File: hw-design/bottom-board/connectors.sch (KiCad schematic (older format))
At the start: 27 parts, among them J1 RJ45_LEDS, J2 JACK_TRS_6PINS, J3 JACK_TRS_6PINS, J4 JACK_TRS_6PINS, J5 JACK_TRS_6PINS, J6 JACK_TRS_6PINS, P5 BARREL_JACK, P6 CONN_02X10, P7 CONN_01X10, P9 CONN_01X03

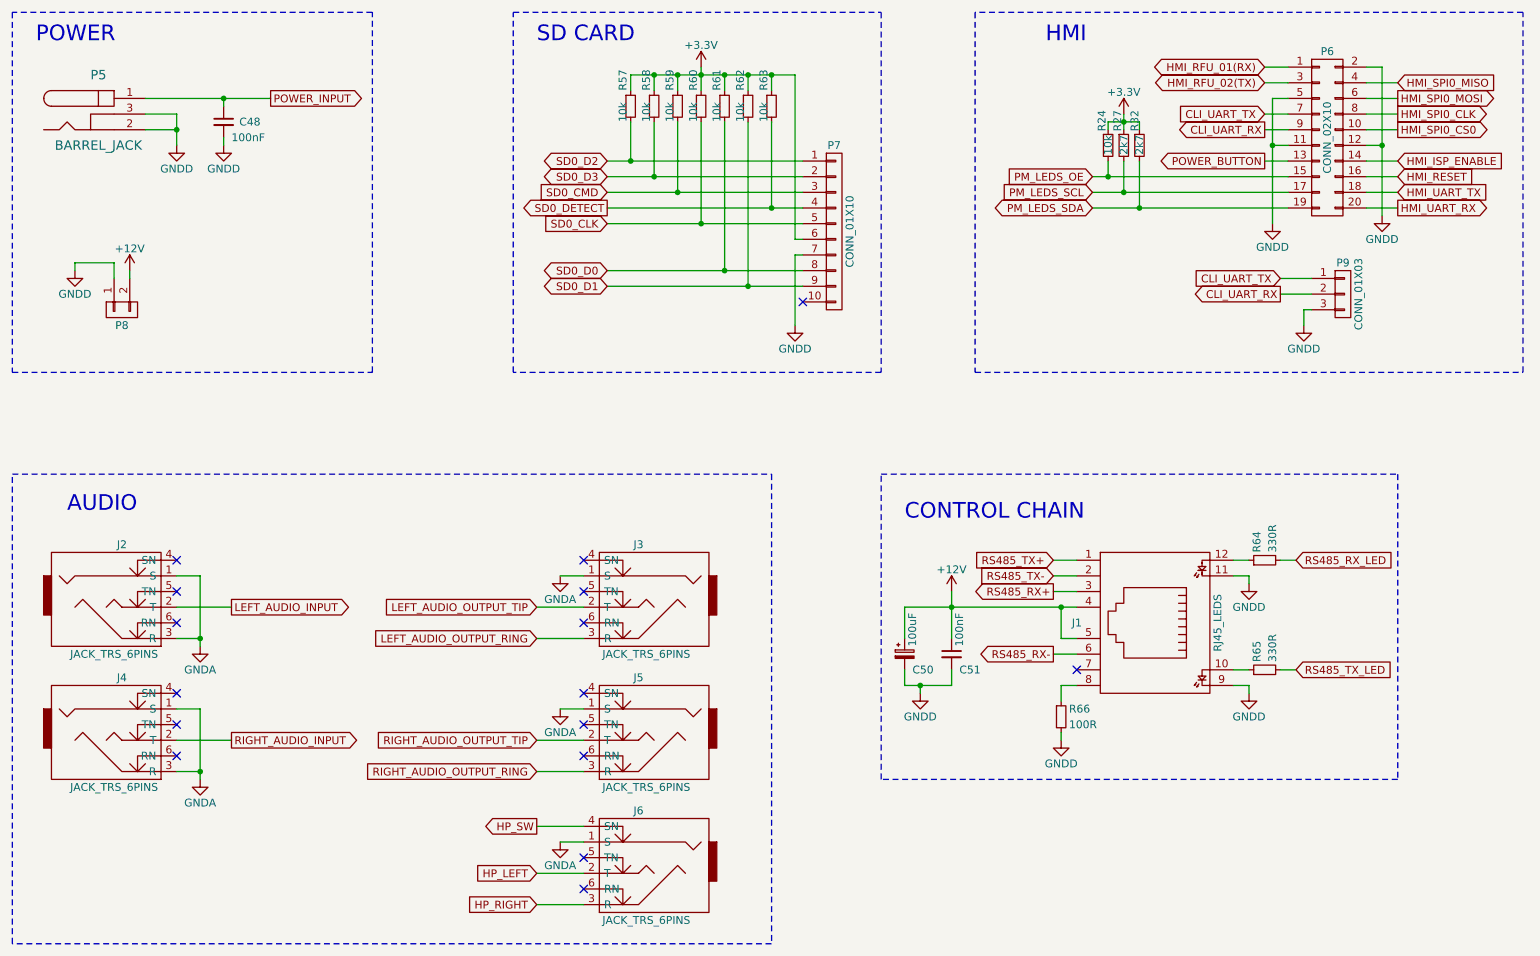
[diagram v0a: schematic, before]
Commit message: sch,bottom-board: ERC passing
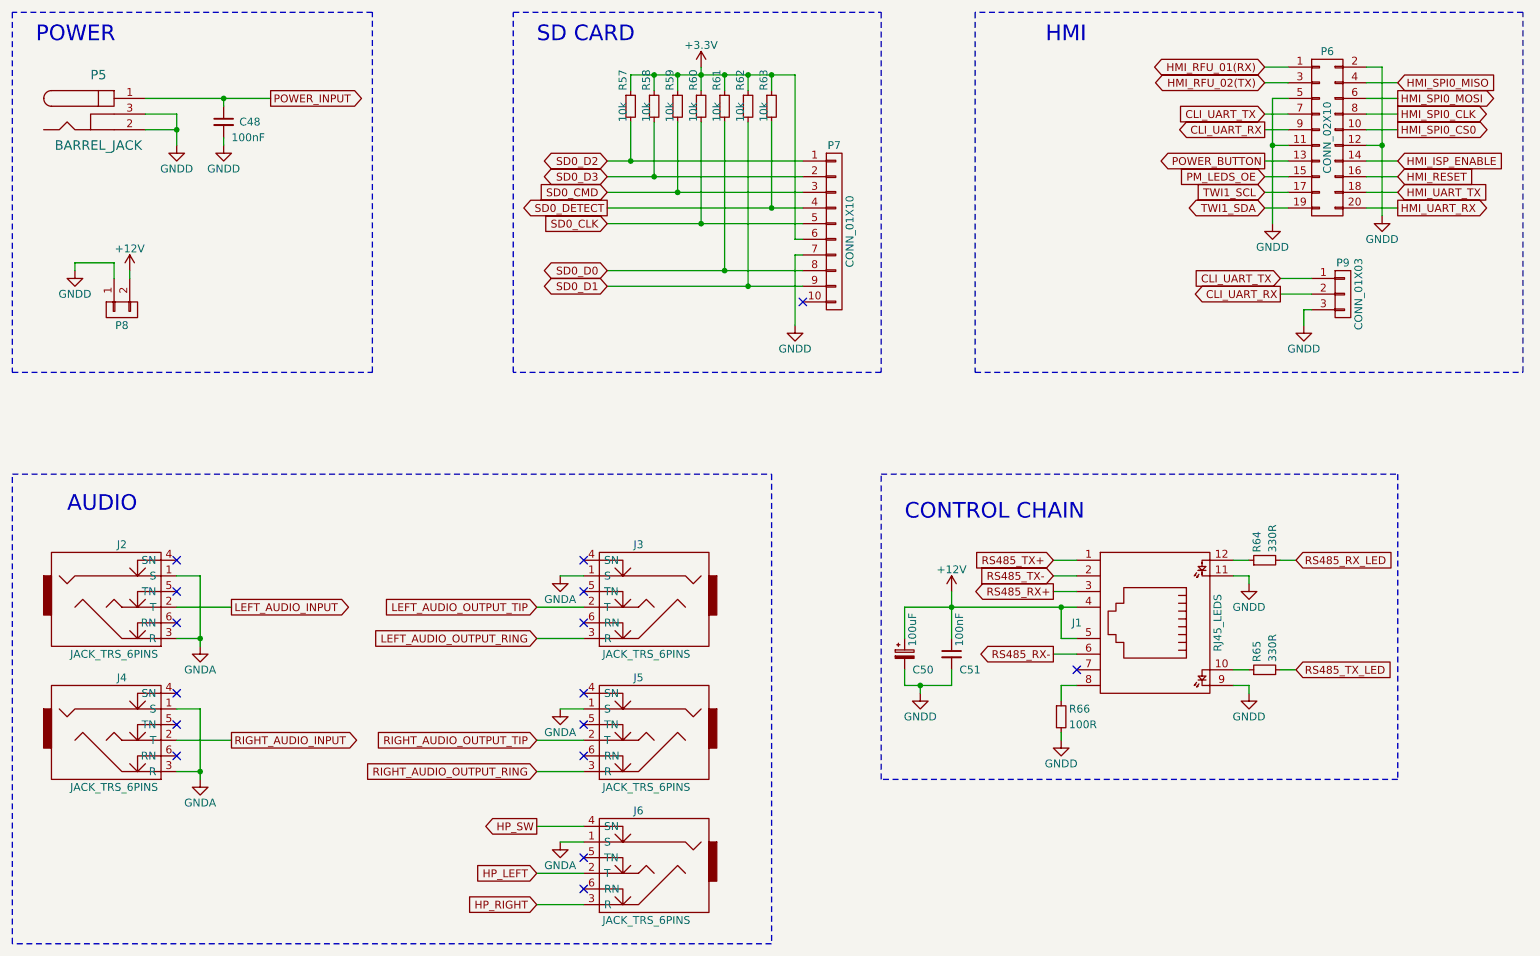
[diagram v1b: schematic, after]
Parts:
- removed R24: 10k, Resistors_SMD:R_0603, symbol R_Small
- removed R27, R32: 2k7, Resistors_SMD:R_0603, symbol R_Small
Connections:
- net PM_LEDS_SCL renamed TWI1_SCL
- net PM_LEDS_SDA renamed TWI1_SDA

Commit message: sch,bottom-board: replacing 2x10 pin header to shrouded version
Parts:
- P6: footprint Pin_Headers:Pin_Header_Straight_2x10 -> footprints:Pin_Header_Straight_2x10_Shrouded
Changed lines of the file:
@@
 F 0 "P6" H 9650 2200 50  0000 C CNN
 F 1 "CONN_02X10" V 9650 1650 50  0000 C CNN
-F 2 "Pin_Headers:Pin_Header_Straight_2x10" H 9650 450 60  0001 C CNN
+F 2 "footprints:Pin_Header_Straight_2x10_Shrouded" H 9650 450 60  0001 C CNN
 F 3 "" H 9650 450 60  0000 C CNN
 F 4 "SBH11-PBPC-D10-ST-BK" H 450 -150 50  0001 C CNN "MPN"

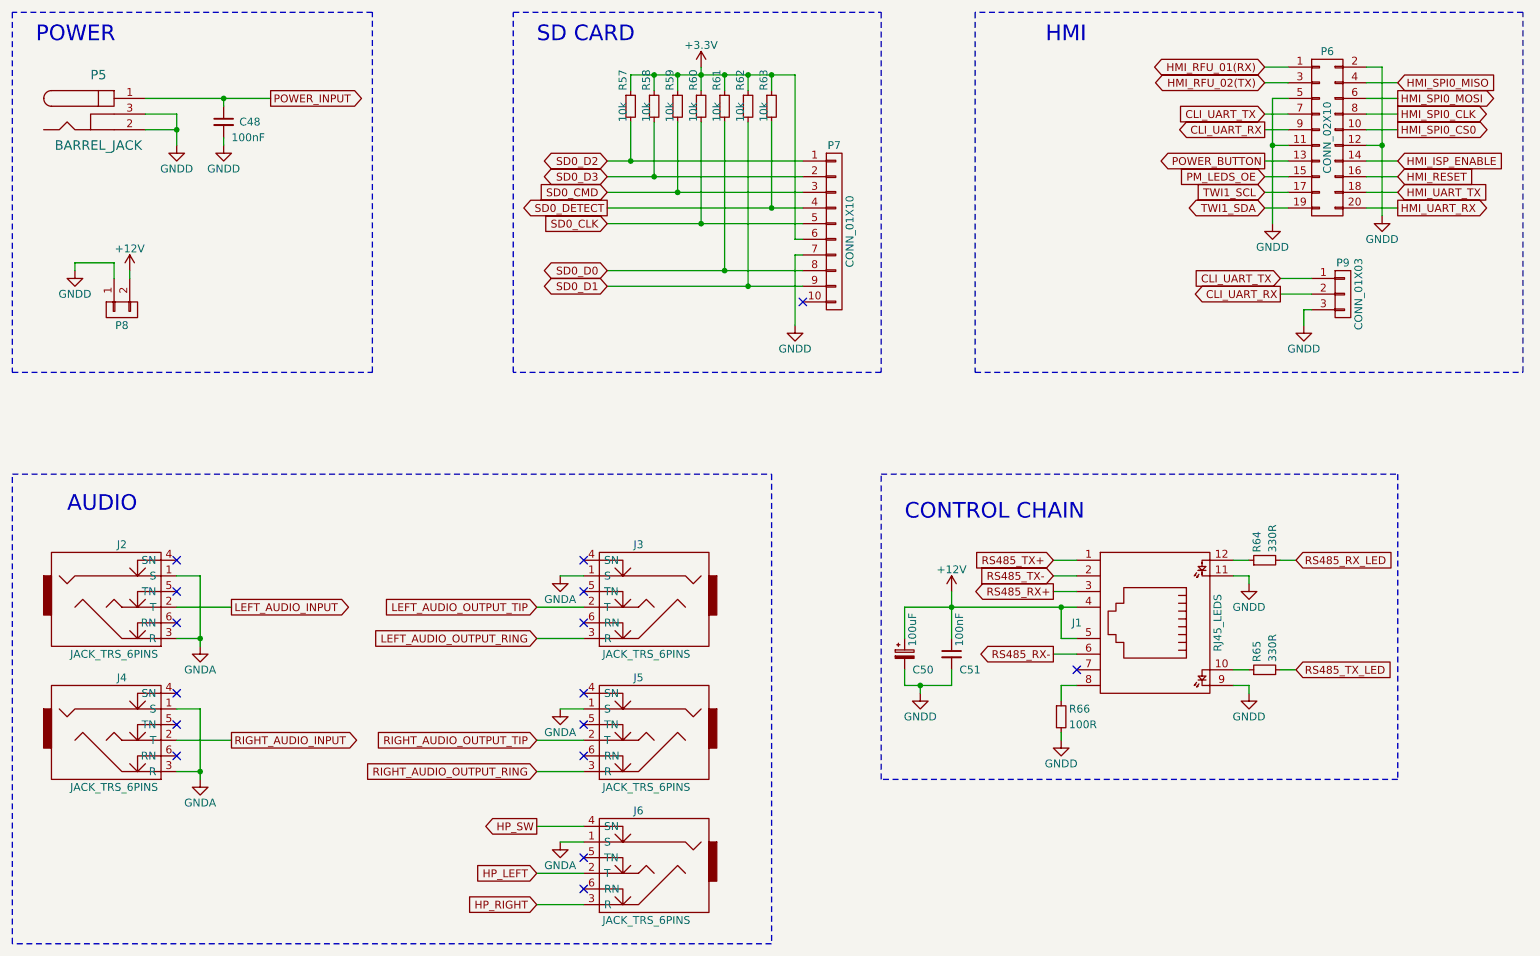
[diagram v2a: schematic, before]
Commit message: sch,bottom-board: new annotation
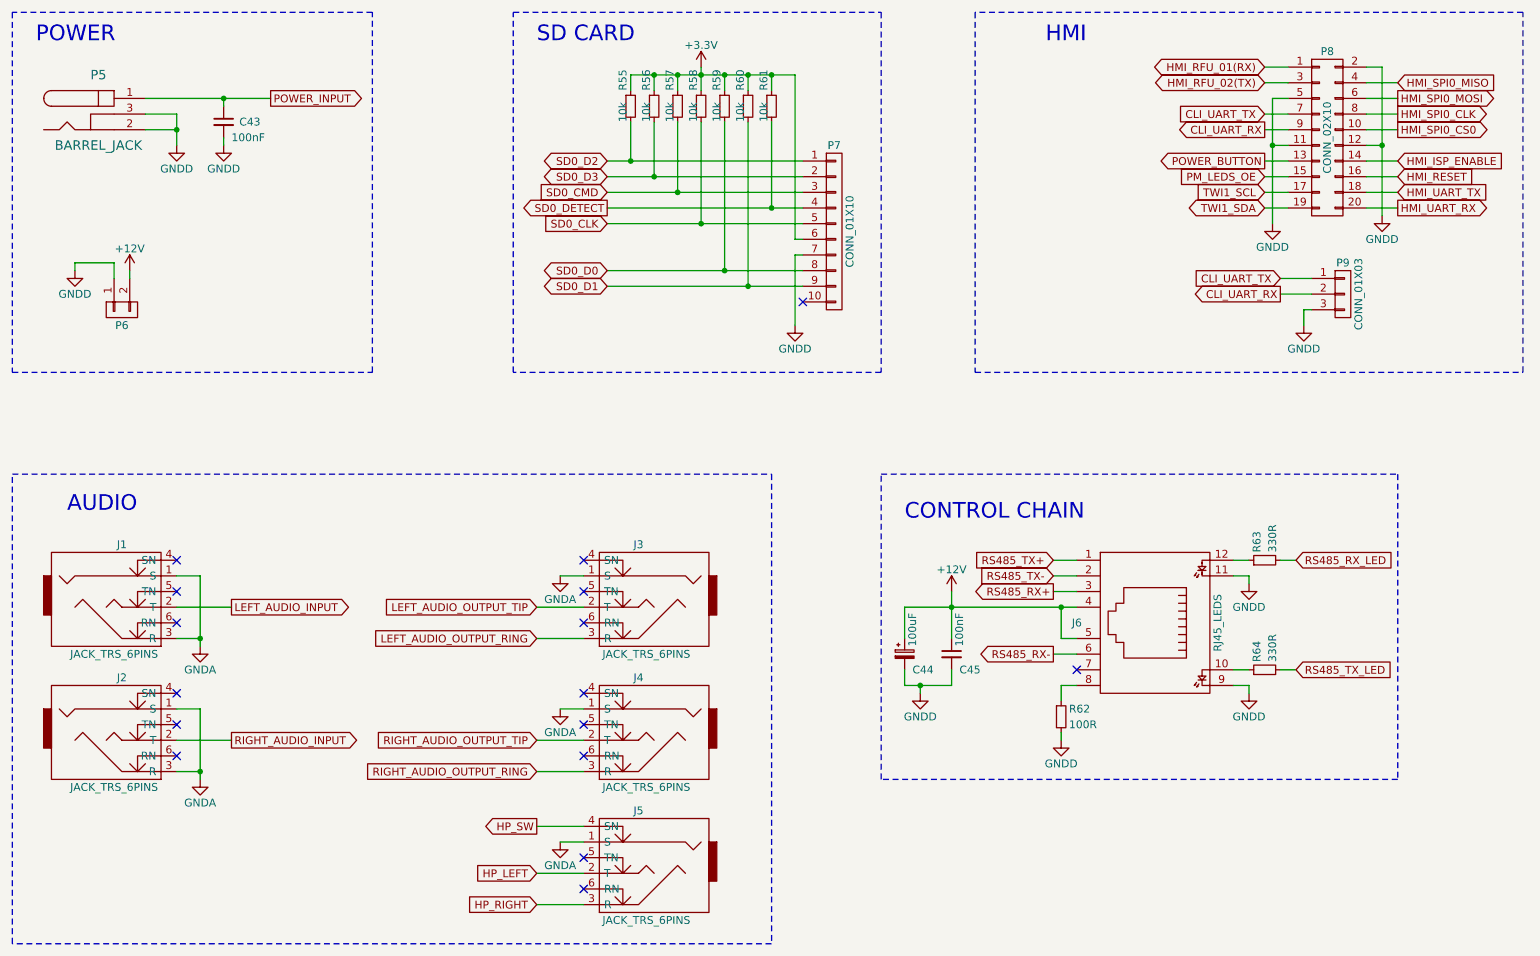
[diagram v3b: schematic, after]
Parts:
- renumbered C48 to C43, C50 to C44, C51 to C45, J2 to J1, J4 to J2, J5 to J4, J6 to J5, J1 to J6, P8 to P6, P6 to P8, R57 to R55, R58 to R56, R59 to R57, R60 to R58, R61 to R59, R62 to R60, R63 to R61, R66 to R62, R64 to R63, R65 to R64
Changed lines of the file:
@@
 $EndComp
 $Comp
-L JACK_TRS_6PINS J4
+L JACK_TRS_6PINS J2
 U 1 1 550C45C0
 P 1900 5500
-F 0 "J4" H 1950 5900 50  0000 C CNN
+F 0 "J2" H 1950 5900 50  0000 C CNN
 F 1 "JACK_TRS_6PINS" H 1900 5200 50  0000 C CNN
 F 2 "Connect:NMJ6HCD2" H 2050 5350 60  0001 C CNN
@@
 $EndComp
 $Comp
-L CONN_02X10 P6
+L CONN_02X10 P8
 U 1 1 550C4B50
 P 9650 1650
-F 0 "P6" H 9650 2200 50  0000 C CNN
+F 0 "P8" H 9650 2200 50  0000 C CNN
 F 1 "CONN_02X10" V 9650 1650 50  0000 C CNN
 F 2 "footprints:Pin_Header_Straight_2x10_Shrouded" H 9650 450 60  0001 C CNN
@@
 $EndComp
 $Comp
-L CONN_01X02 P8
+L CONN_01X02 P6
 U 1 1 550C4D2F
 P 1950 2750
-F 0 "P8" V 2050 2750 50  0000 C CNN
+F 0 "P6" V 2050 2750 50  0000 C CNN
 F 1 "~" V 2050 2750 50  0000 C CNN
 F 2 "footprints:Pin_Header_Straight_1x02_Pitch2.00mm_Shrouded" H 1950 2750 60  0001 C CNN
@@
 $EndComp
 $Comp
-L C_Small C48
+L C_Small C43
 U 1 1 550C63C7
 P 2600 1550
-F 0 "C48" H 2700 1550 50  0000 L CNN
+F 0 "C43" H 2700 1550 50  0000 L CNN
 F 1 "100nF" H 2650 1450 50  0000 L CNN
 F 2 "Capacitors_SMD:C_0603" H 2600 1550 60  0001 C CNN
@@
 $EndComp
 $Comp
-L JACK_TRS_6PINS J2
+L JACK_TRS_6PINS J1
 U 1 1 550C776E
 P 1900 4650
-F 0 "J2" H 1950 5050 50  0000 C CNN
+F 0 "J1" H 1950 5050 50  0000 C CNN
 F 1 "JACK_TRS_6PINS" H 1900 4350 50  0000 C CNN
 F 2 "Connect:NMJ6HCD2" H 2050 4500 60  0001 C CNN
@@
 $EndComp
 $Comp
-L JACK_TRS_6PINS J5
+L JACK_TRS_6PINS J4
 U 1 1 550C79F9
 P 5300 5500
-F 0 "J5" H 5350 5900 50  0000 C CNN
+F 0 "J4" H 5350 5900 50  0000 C CNN
 F 1 "JACK_TRS_6PINS" H 5300 5200 50  0000 C CNN
 F 2 "Connect:NMJ6HCD2" H 5450 5350 60  0001 C CNN
@@
 $EndComp
 $Comp
-L JACK_TRS_6PINS J6
+L JACK_TRS_6PINS J5
 U 1 1 550C7A43
 P 5300 6350
-F 0 "J6" H 5350 6750 50  0000 C CNN
+F 0 "J5" H 5350 6750 50  0000 C CNN
 F 1 "JACK_TRS_6PINS" H 5300 6050 50  0000 C CNN
 F 2 "Connect:NMJ6HCD2" H 5450 6200 60  0001 C CNN
@@
 $EndComp
 $Comp
-L R_Small R66
+L R_Small R62
 U 1 1 550C9A10
 P 7950 5350
-F 0 "R66" H 8000 5400 50  0000 L CNN
+F 0 "R62" H 8000 5400 50  0000 L CNN
 F 1 "100R" H 8000 5300 50  0000 L CNN
 F 2 "Resistors_SMD:R_0603" H 7950 5350 60  0001 C CNN
@@
 $EndComp
 $Comp
-L C_Small C51
+L C_Small C45
 U 1 1 550C9E35
 P 7250 4950
-F 0 "C51" H 7300 4850 50  0000 L CNN
+F 0 "C45" H 7300 4850 50  0000 L CNN
 F 1 "100nF" V 7300 5000 50  0000 L CNN
 F 2 "Capacitors_SMD:C_0603" H 7250 4950 60  0001 C CNN
@@
 $EndComp
 $Comp
-L CP_Small C50
+L CP_Small C44
 U 1 1 550C9E8B
 P 6950 4950
-F 0 "C50" H 7000 4850 50  0000 L CNN
+F 0 "C44" H 7000 4850 50  0000 L CNN
 F 1 "100uF" V 7000 5000 50  0000 L CNN
 F 2 "Capacitors_SMD:c_elec_6.3x5.3" H 6950 4950 60  0001 C CNN
@@
 $EndComp
 $Comp
-L R_Small R57
+L R_Small R55
 U 1 1 550B9034
 P 5200 1450
-F 0 "R57" V 5150 1550 50  0000 L CNN
+F 0 "R55" V 5150 1550 50  0000 L CNN
 F 1 "10k" V 5150 1350 50  0000 L CNN
 F 2 "Resistors_SMD:R_0603" H 5200 1450 60  0001 C CNN
@@
 $EndComp
 $Comp
-L R_Small R58
+L R_Small R56
 U 1 1 550B9CEA
 P 5350 1450
-F 0 "R58" V 5300 1550 50  0000 L CNN
+F 0 "R56" V 5300 1550 50  0000 L CNN
 F 1 "10k" V 5300 1350 50  0000 L CNN
 F 2 "Resistors_SMD:R_0603" H 5350 1450 60  0001 C CNN
@@
 $EndComp
 $Comp
-L R_Small R59
+L R_Small R57
 U 1 1 550B9D20
 P 5500 1450
-F 0 "R59" V 5450 1550 50  0000 L CNN
+F 0 "R57" V 5450 1550 50  0000 L CNN
 F 1 "10k" V 5450 1350 50  0000 L CNN
 F 2 "Resistors_SMD:R_0603" H 5500 1450 60  0001 C CNN
@@
 $EndComp
 $Comp
-L R_Small R60
+L R_Small R58
 U 1 1 550B9D5C
 P 5650 1450
-F 0 "R60" V 5600 1550 50  0000 L CNN
+F 0 "R58" V 5600 1550 50  0000 L CNN
 F 1 "10k" V 5600 1350 50  0000 L CNN
 F 2 "Resistors_SMD:R_0603" H 5650 1450 60  0001 C CNN
@@
 $EndComp
 $Comp
-L R_Small R61
+L R_Small R59
 U 1 1 550B9D96
 P 5800 1450
-F 0 "R61" V 5750 1550 50  0000 L CNN
+F 0 "R59" V 5750 1550 50  0000 L CNN
 F 1 "10k" V 5750 1350 50  0000 L CNN
 F 2 "Resistors_SMD:R_0603" H 5800 1450 60  0001 C CNN
@@
 $EndComp
 $Comp
-L R_Small R62
+L R_Small R60
 U 1 1 550B9DD2
 P 5950 1450
-F 0 "R62" V 5900 1550 50  0000 L CNN
+F 0 "R60" V 5900 1550 50  0000 L CNN
 F 1 "10k" V 5900 1350 50  0000 L CNN
 F 2 "Resistors_SMD:R_0603" H 5950 1450 60  0001 C CNN
@@
 $EndComp
 $Comp
-L R_Small R63
+L R_Small R61
 U 1 1 550BB308
 P 6100 1450
-F 0 "R63" V 6050 1550 50  0000 L CNN
+F 0 "R61" V 6050 1550 50  0000 L CNN
 F 1 "10k" V 6050 1350 50  0000 L CNN
 F 2 "Resistors_SMD:R_0603" H 6100 1450 60  0001 C CNN
@@
 $EndComp
 $Comp
-L RJ45_LEDS J1
+L RJ45_LEDS J6
 U 1 1 5519BC3F
 P 8550 4750
-F 0 "J1" V 8550 4250 50  0000 C CNN
+F 0 "J6" V 8550 4250 50  0000 C CNN
 F 1 "RJ45_LEDS" H 8550 5150 50  0000 C CNN
 F 2 "Connect:RJHSE538X" H 8550 4700 60  0001 C CNN
@@
 $EndComp
 $Comp
-L R_Small R64
+L R_Small R63
 U 1 1 551A2D92
 P 9250 4350
-F 0 "R64" H 9300 4400 50  0000 L CNN
+F 0 "R63" H 9300 4400 50  0000 L CNN
 F 1 "330R" H 9300 4300 50  0000 L CNN
 F 2 "Resistors_SMD:R_0603" H 9250 4350 60  0001 C CNN
@@
 $EndComp
 $Comp
-L R_Small R65
+L R_Small R64
 U 1 1 551A4873
 P 9250 5050
-F 0 "R65" H 9300 5100 50  0000 L CNN
+F 0 "R64" H 9300 5100 50  0000 L CNN
 F 1 "330R" H 9300 5000 50  0000 L CNN
 F 2 "Resistors_SMD:R_0603" H 9250 5050 60  0001 C CNN

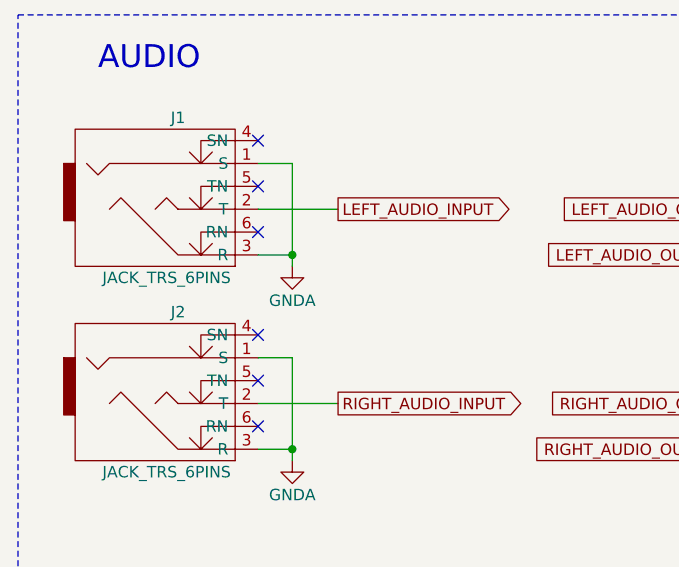
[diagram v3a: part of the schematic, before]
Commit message: sch,bottom-board: connecting audio inputs to ground when jack isn't plugged
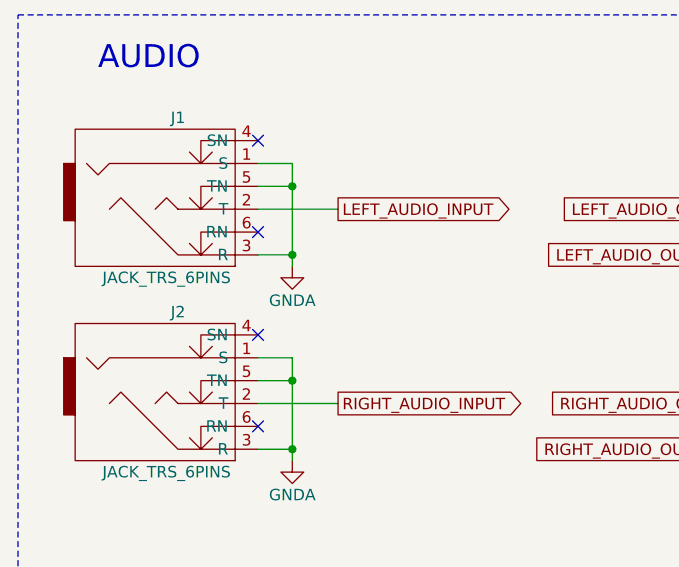
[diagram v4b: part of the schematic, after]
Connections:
- net GNDA: now also J1.5 (TN), J2.5 (TN)
- no-connect marks 16 -> 14
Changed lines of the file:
@@
 NoConn ~ 4900 5600
 NoConn ~ 2300 4350
-NoConn ~ 2300 4550
 NoConn ~ 2300 4750
 NoConn ~ 2300 5600
-NoConn ~ 2300 5400
 NoConn ~ 2300 5200
 $Comp
@@
 	6100 1550 6100 2100
 Connection ~ 6100 2100
+Wire Wire Line
+	2300 5400 2450 5400
+Connection ~ 2450 5400
+Wire Wire Line
+	2300 4550 2450 4550
+Connection ~ 2450 4550
 $EndSCHEMATC
